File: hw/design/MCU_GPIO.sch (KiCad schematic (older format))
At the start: 1 part

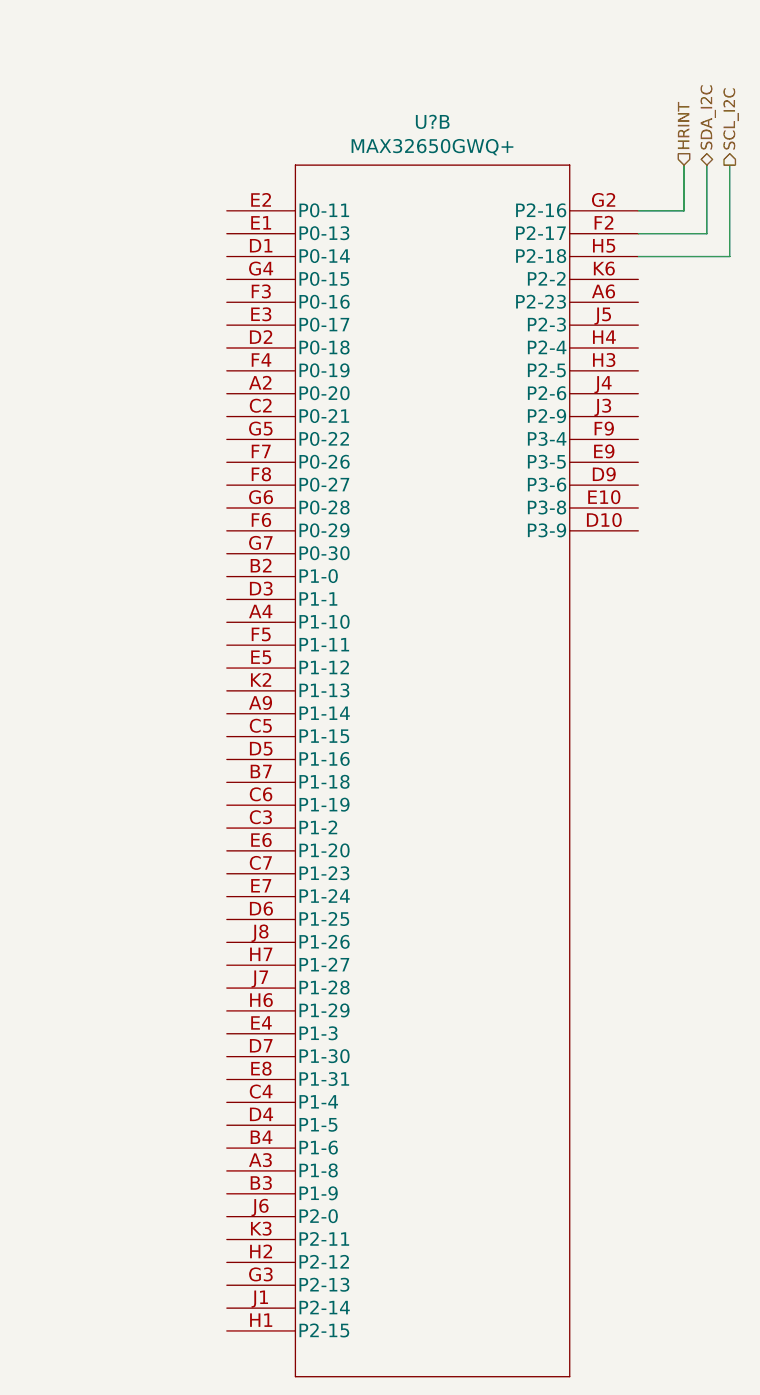
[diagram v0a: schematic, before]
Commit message: schematic/parts: SD Card
I have elected to move from writing notes to writing git commits instead. It may be easier to read for some.
Anyhow, I decided to research a little bit for a thinner SD card mount to improve my odds of the HR sensor being the tallest part on one side of the PCB.
Quite unlikely, but still. Didn't take much time at all and had to do some digging around for how the SD spec even works electronically.
Notes file will still keep track of all the parts, I might rename the file to "parts" as that's its most useful case other than me thinking on pixel.

Still workin'
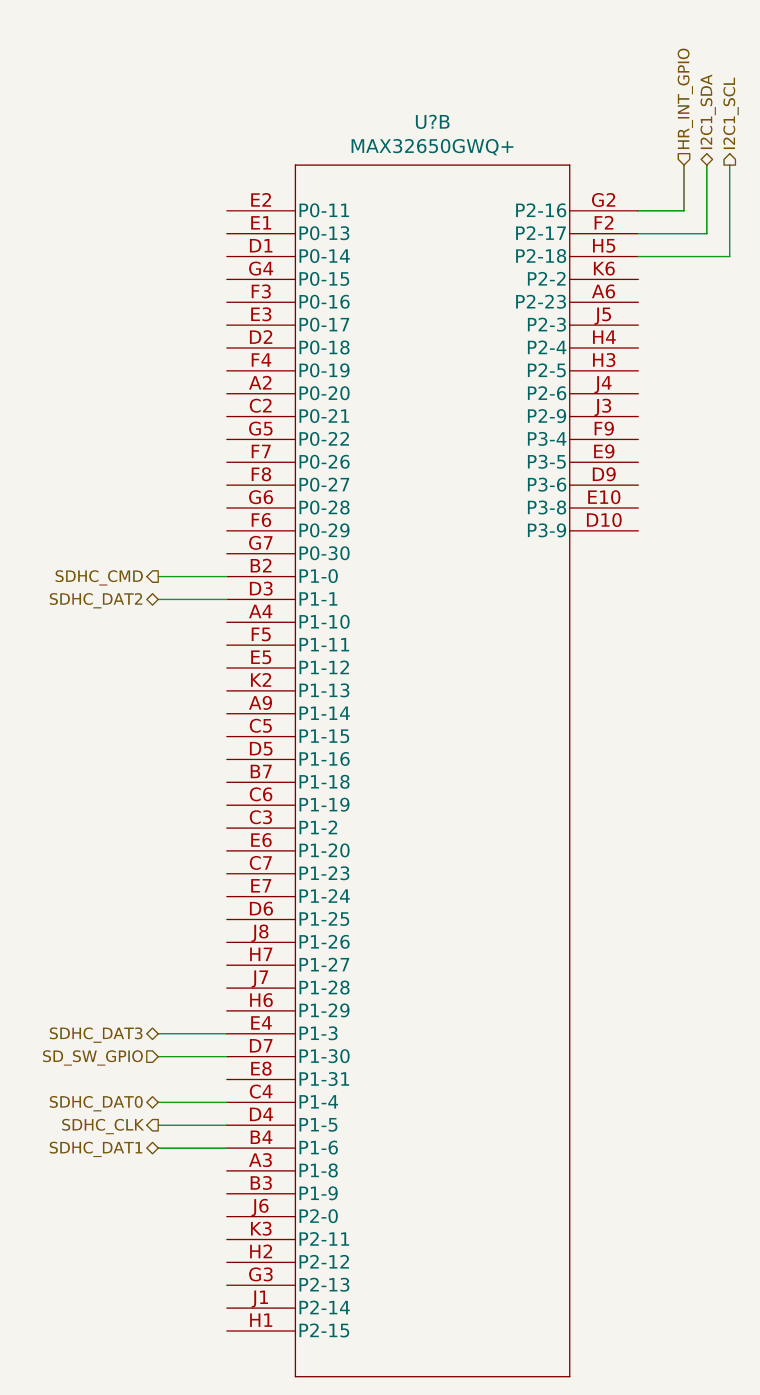
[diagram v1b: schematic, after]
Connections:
- net SDHC_CMD: now reaches U?.B2 (P1-0)
- net SDHC_DAT1: now reaches U?.B4 (P1-6)
- net SDHC_DAT0: now reaches U?.C4 (P1-4)
- net SDHC_DAT2: now reaches U?.D3 (P1-1)
- net SDHC_CLK: now reaches U?.D4 (P1-5)
- net SD_SW_GPIO: now reaches U?.D7 (P1-30)
- net SDHC_DAT3: now reaches U?.E4 (P1-3)
- net HRINT renamed HR_INT_GPIO
- net SCL_I2C renamed I2C1_SCL
- net SDA_I2C renamed I2C1_SDA
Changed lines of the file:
@@
 $Descr A4 11693 8268
 encoding utf-8
-Sheet 3 5
+Sheet 3 6
 Title ""
 Date ""
@@
 	6800 1500 6800 1300
 Text HLabel 6800 1300 1    50   Input ~ 0
-HRINT
+HR_INT_GPIO
 Text HLabel 6900 1300 1    50   BiDi ~ 0
-SDA_I2C
+I2C1_SDA
 Text HLabel 7000 1300 1    50   Output ~ 0
-SCL_I2C
+I2C1_SCL
+Wire Wire Line
+	4500 3100 4800 3100
+Wire Wire Line
+	4500 3200 4800 3200
+Wire Wire Line
+	4800 5100 4500 5100
+Wire Wire Line
+	4800 5400 4500 5400
+Wire Wire Line
+	4800 5500 4500 5500
+Wire Wire Line
+	4800 5600 4500 5600
+Wire Wire Line
+	4800 5200 4500 5200
+Text HLabel 4500 5200 0    50   Input ~ 0
+SD_SW_GPIO
+Text HLabel 4500 5400 0    50   BiDi ~ 0
+SDHC_DAT0
+Text HLabel 4500 5500 0    50   Output ~ 0
+SDHC_CLK
+Text HLabel 4500 5600 0    50   BiDi ~ 0
+SDHC_DAT1
+Text HLabel 4500 5100 0    50   BiDi ~ 0
+SDHC_DAT3
+Text HLabel 4500 3100 0    50   Output ~ 0
+SDHC_CMD
+Text HLabel 4500 3200 0    50   BiDi ~ 0
+SDHC_DAT2
 $EndSCHEMATC
